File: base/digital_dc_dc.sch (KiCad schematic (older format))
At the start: 33 parts

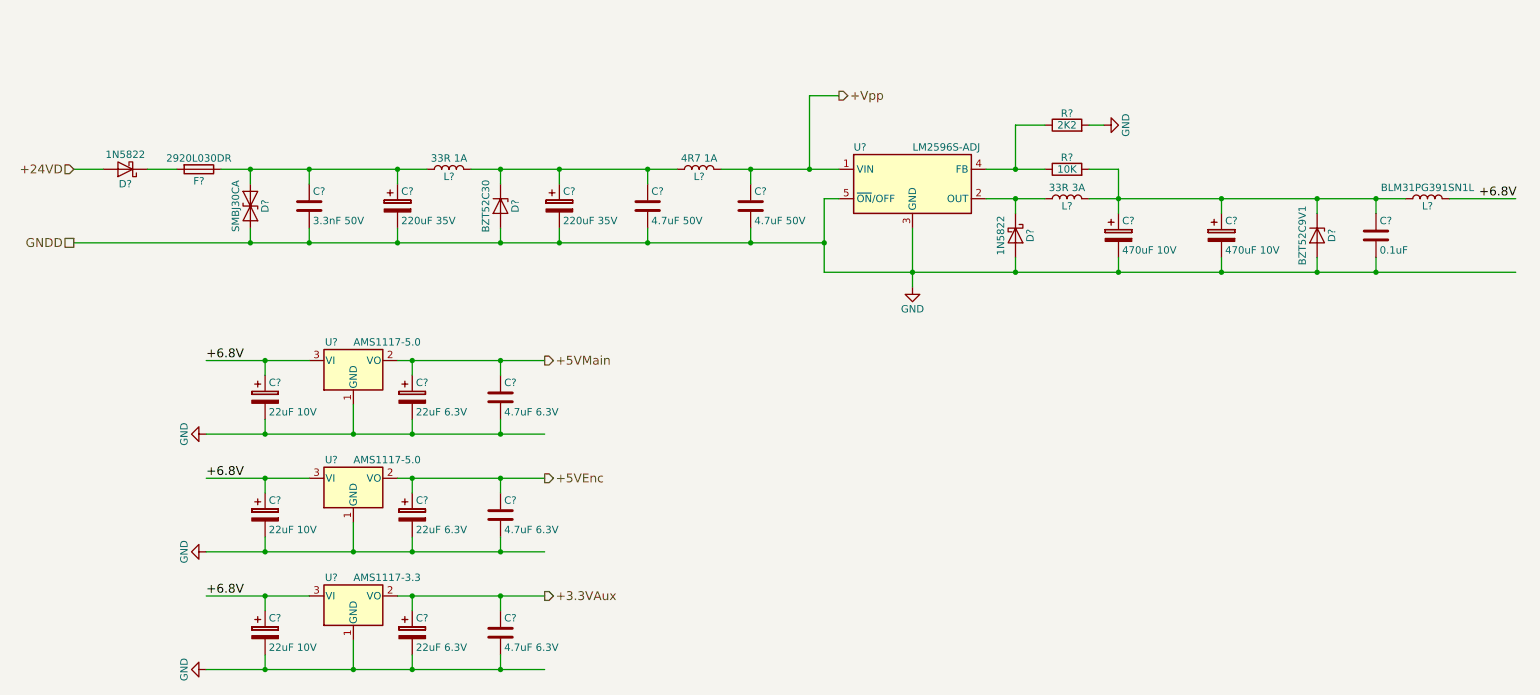
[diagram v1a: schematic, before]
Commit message: Update base board: 1. Add extra analog voltage input to core board.   -> update pinmux 2. Assign most footprints. 3. Generate netlist. 4. Add core_sf board. 5. Add kicad_symbols library submodule.
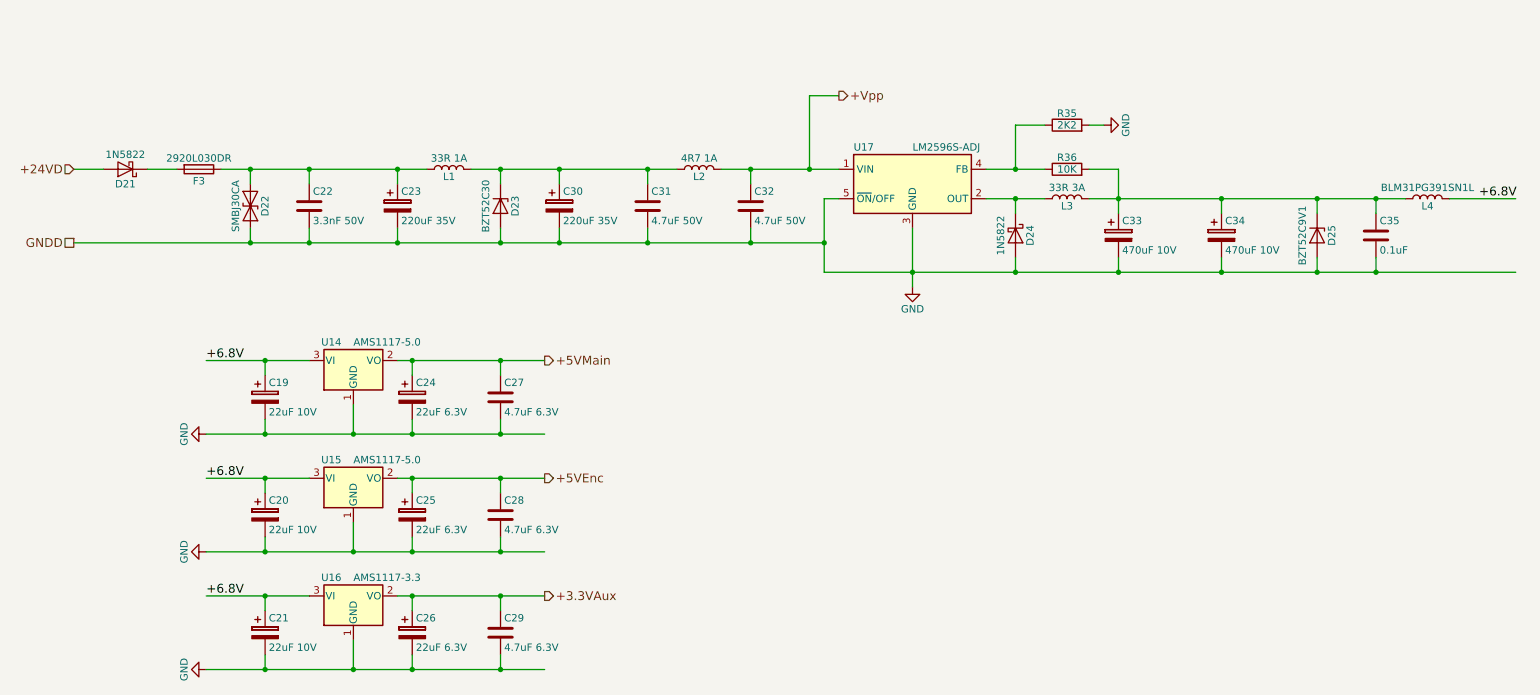
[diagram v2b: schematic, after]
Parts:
- gave numbers to parts that had none: 33
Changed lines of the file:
@@
 GNDD
 $Comp
-L 1N5822 D?
+L 1N5822 D21
 U 1 1 5A392E0A
 P 1550 3000
-F 0 "D?" H 1550 3100 50  0000 C CNN
+F 0 "D21" H 1550 3100 50  0000 C CNN
 F 1 "1N5822" H 1550 2900 50  0000 C CNN
 F 2 "Diode_SMD:D_SMA" H 1550 2825 50  0001 C CNN
@@
 $EndComp
 $Comp
-L Fuse F?
+L Fuse F3
 U 1 1 5A392F16
 P 2050 3000
-F 0 "F?" V 2130 3000 50  0000 C CNN
+F 0 "F3" V 2130 3000 50  0000 C CNN
 F 1 "2920L030DR" V 1975 3000 50  0000 C CNN
 F 2 "Fuse:Fuse_2920_7451Metric" V 1980 3000 50  0001 C CNN
@@
 $EndComp
 $Comp
-L D_TVS D?
+L D_TVS D22
 U 1 1 5A3934E7
 P 2400 3250
-F 0 "D?" H 2400 3350 50  0000 C CNN
+F 0 "D22" H 2400 3350 50  0000 C CNN
 F 1 "SMBJ30CA" H 2400 3150 50  0000 C CNN
 F 2 "Diode_SMD:D_SMB" H 2400 3250 50  0001 C CNN
@@
 $EndComp
 $Comp
-L C C?
+L C C22
 U 1 1 5A393804
 P 2800 3250
-F 0 "C?" H 2825 3350 50  0000 L CNN
+F 0 "C22" H 2825 3350 50  0000 L CNN
 F 1 "3.3nF 50V" H 2825 3150 50  0000 L CNN
 F 2 "Capacitor_SMD:C_0603_1608Metric" H 2838 3100 50  0001 C CNN
@@
 $EndComp
 $Comp
-L CP C?
+L CP C23
 U 1 1 5A393B3D
 P 3400 3250
-F 0 "C?" H 3425 3350 50  0000 L CNN
+F 0 "C23" H 3425 3350 50  0000 L CNN
 F 1 "220uF 35V" H 3425 3150 50  0000 L CNN
 F 2 "Capacitor_SMD:CP_Elec_8x10" H 3438 3100 50  0001 C CNN
@@
 $EndComp
 $Comp
-L L L?
+L L L1
 U 1 1 5A3940E0
 P 3750 3000
-F 0 "L?" V 3700 3000 50  0000 C CNN
+F 0 "L1" V 3700 3000 50  0000 C CNN
 F 1 "33R 1A" V 3825 3000 50  0000 C CNN
 F 2 "Inductor_SMD:L_7.3x7.3_H3.5" H 3750 3000 50  0001 C CNN
@@
 $EndComp
 $Comp
-L D_Zener D?
+L D_Zener D23
 U 1 1 5A394214
 P 4100 3250
-F 0 "D?" H 4100 3350 50  0000 C CNN
+F 0 "D23" H 4100 3350 50  0000 C CNN
 F 1 "BZT52C30" H 4100 3150 50  0000 C CNN
 F 2 "Diode_SMD:D_SOD-123" H 4100 3250 50  0001 C CNN
@@
 $EndComp
 $Comp
-L CP C?
+L CP C30
 U 1 1 5A394320
 P 4500 3250
-F 0 "C?" H 4525 3350 50  0000 L CNN
+F 0 "C30" H 4525 3350 50  0000 L CNN
 F 1 "220uF 35V" H 4525 3150 50  0000 L CNN
 F 2 "Capacitor_SMD:CP_Elec_8x10" H 4538 3100 50  0001 C CNN
@@
 $EndComp
 $Comp
-L C C?
+L C C31
 U 1 1 5A394607
 P 5100 3250
-F 0 "C?" H 5125 3350 50  0000 L CNN
+F 0 "C31" H 5125 3350 50  0000 L CNN
 F 1 "4.7uF 50V" H 5125 3150 50  0000 L CNN
 F 2 "Capacitor_SMD:C_1210_3225Metric" H 5138 3100 50  0001 C CNN
@@
 $EndComp
 $Comp
-L L L?
+L L L2
 U 1 1 5A394796
 P 5450 3000
-F 0 "L?" V 5400 3000 50  0000 C CNN
+F 0 "L2" V 5400 3000 50  0000 C CNN
 F 1 "4R7 1A" V 5525 3000 50  0000 C CNN
 F 2 "Inductor_SMD:L_Taiyo-Yuden_MD-3030" H 5450 3000 50  0001 C CNN
@@
 $EndComp
 $Comp
-L C C?
+L C C32
 U 1 1 5A394844
 P 5800 3250
-F 0 "C?" H 5825 3350 50  0000 L CNN
+F 0 "C32" H 5825 3350 50  0000 L CNN
 F 1 "4.7uF 50V" H 5825 3150 50  0000 L CNN
 F 2 "Capacitor_SMD:C_1210_3225Metric" H 5838 3100 50  0001 C CNN
@@
 $EndComp
 $Comp
-L LM2596S-ADJ U?
+L LM2596S-ADJ U17
 U 1 1 5A395D36
 P 6900 3100
-F 0 "U?" H 6500 3350 50  0000 L CNN
+F 0 "U17" H 6500 3350 50  0000 L CNN
 F 1 "LM2596S-ADJ" H 6900 3350 50  0000 L CNN
 F 2 "Package_TO_SOT_SMD:TO-263-5_TabPin3" H 6950 2850 50  0001 L CIN
@@
 $EndComp
 $Comp
-L 1N5822 D?
+L 1N5822 D24
 U 1 1 5A395F02
 P 7600 3450
-F 0 "D?" H 7600 3550 50  0000 C CNN
+F 0 "D24" H 7600 3550 50  0000 C CNN
 F 1 "1N5822" H 7600 3350 50  0000 C CNN
 F 2 "Diode_SMD:D_SMA" H 7600 3275 50  0001 C CNN
@@
 $EndComp
 $Comp
-L L L?
+L L L3
 U 1 1 5A396123
 P 7950 3200
-F 0 "L?" V 7900 3200 50  0000 C CNN
+F 0 "L3" V 7900 3200 50  0000 C CNN
 F 1 "33R 3A" V 8025 3200 50  0000 C CNN
 F 2 "Inductor_SMD:L_12x12mm_h8mm" H 7950 3200 50  0001 C CNN
@@
 $EndComp
 $Comp
-L R R?
+L R R36
 U 1 1 5A396200
 P 7950 3000
-F 0 "R?" V 8030 3000 50  0000 C CNN
+F 0 "R36" V 8030 3000 50  0000 C CNN
 F 1 "10K" V 7950 3000 50  0000 C CNN
 F 2 "Resistor_SMD:R_0603_1608Metric" V 7880 3000 50  0001 C CNN
@@
 $EndComp
 $Comp
-L R R?
+L R R35
 U 1 1 5A396375
 P 7950 2700
-F 0 "R?" V 8030 2700 50  0000 C CNN
+F 0 "R35" V 8030 2700 50  0000 C CNN
 F 1 "2K2" V 7950 2700 50  0000 C CNN
 F 2 "Resistor_SMD:R_0603_1608Metric" V 7880 2700 50  0001 C CNN
@@
 $EndComp
 $Comp
-L GND #PWR?
+L GND #PWR020
 U 1 1 5A3963F4
 P 6900 3800
-F 0 "#PWR?" H 6900 3550 50  0001 C CNN
+F 0 "#PWR020" H 6900 3550 50  0001 C CNN
 F 1 "GND" H 6900 3650 50  0000 C CNN
 F 2 "" H 6900 3800 50  0001 C CNN
@@
 $EndComp
 $Comp
-L GND #PWR?
+L GND #PWR021
 U 1 1 5A3964B9
 P 8200 2700
-F 0 "#PWR?" H 8200 2450 50  0001 C CNN
+F 0 "#PWR021" H 8200 2450 50  0001 C CNN
 F 1 "GND" H 8200 2550 50  0000 C CNN
 F 2 "" H 8200 2700 50  0001 C CNN
@@
 $EndComp
 $Comp
-L CP C?
+L CP C33
 U 1 1 5A3964F4
 P 8300 3450
-F 0 "C?" H 8325 3550 50  0000 L CNN
+F 0 "C33" H 8325 3550 50  0000 L CNN
 F 1 "470uF 10V" H 8325 3350 50  0000 L CNN
 F 2 "Capacitor_SMD:CP_Elec_8x10" H 8338 3300 50  0001 C CNN
@@
 $EndComp
 $Comp
-L D_Zener D?
+L D_Zener D25
 U 1 1 5A396751
 P 9650 3450
-F 0 "D?" H 9650 3550 50  0000 C CNN
+F 0 "D25" H 9650 3550 50  0000 C CNN
 F 1 "BZT52C9V1" H 9650 3350 50  0000 C CNN
 F 2 "Diode_SMD:D_SOD-123" H 9650 3450 50  0001 C CNN
@@
 $EndComp
 $Comp
-L C C?
+L C C35
 U 1 1 5A396963
 P 10050 3450
-F 0 "C?" H 10075 3550 50  0000 L CNN
+F 0 "C35" H 10075 3550 50  0000 L CNN
 F 1 "0.1uF" H 10075 3350 50  0000 L CNN
 F 2 "Capacitor_SMD:C_0603_1608Metric" H 10088 3300 50  0001 C CNN
@@
 $EndComp
 $Comp
-L L L?
+L L L4
 U 1 1 5A396C17
 P 10400 3200
-F 0 "L?" V 10350 3200 50  0000 C CNN
+F 0 "L4" V 10350 3200 50  0000 C CNN
 F 1 "BLM31PG391SN1L" V 10475 3200 50  0000 C CNN
 F 2 "Inductor_SMD:L_1206_3216Metric" H 10400 3200 50  0001 C CNN
@@
 +6.8V
 $Comp
-L CP C?
+L CP C19
 U 1 1 5A3971EB
 P 2500 4550
-F 0 "C?" H 2525 4650 50  0000 L CNN
+F 0 "C19" H 2525 4650 50  0000 L CNN
 F 1 "22uF 10V" H 2525 4450 50  0000 L CNN
 F 2 "Capacitor_Tantalum_SMD:CP_EIA-3216-18_Kemet-A" H 2538 4400 50  0001 C CNN
@@
 $EndComp
 $Comp
-L AP1117-15 U?
+L AP1117-15 U14
 U 1 1 5A398264
 P 3100 4300
-F 0 "U?" H 2950 4425 50  0000 C CNN
+F 0 "U14" H 2950 4425 50  0000 C CNN
 F 1 "AMS1117-5.0" H 3100 4425 50  0000 L CNN
 F 2 "Package_TO_SOT_SMD:SOT-223" H 3100 4500 50  0001 C CNN
@@
 +6.8V
 $Comp
-L GND #PWR?
+L GND #PWR022
 U 1 1 5A3987CE
 P 2100 4800
-F 0 "#PWR?" H 2100 4550 50  0001 C CNN
+F 0 "#PWR022" H 2100 4550 50  0001 C CNN
 F 1 "GND" H 2100 4650 50  0000 C CNN
 F 2 "" H 2100 4800 50  0001 C CNN
@@
 $EndComp
 $Comp
-L CP C?
+L CP C24
 U 1 1 5A3988D5
 P 3500 4550
-F 0 "C?" H 3525 4650 50  0000 L CNN
+F 0 "C24" H 3525 4650 50  0000 L CNN
 F 1 "22uF 6.3V" H 3525 4450 50  0000 L CNN
 F 2 "Capacitor_Tantalum_SMD:CP_EIA-3216-18_Kemet-A" H 3538 4400 50  0001 C CNN
@@
 $EndComp
 $Comp
-L C C?
+L C C27
 U 1 1 5A398AEE
 P 4100 4550
-F 0 "C?" H 4125 4650 50  0000 L CNN
+F 0 "C27" H 4125 4650 50  0000 L CNN
 F 1 "4.7uF 6.3V" H 4125 4450 50  0000 L CNN
 F 2 "Capacitor_SMD:C_0603_1608Metric" H 4138 4400 50  0001 C CNN
@@
 $EndComp
 $Comp
-L CP C?
+L CP C20
 U 1 1 5A398DF8
 P 2500 5350
-F 0 "C?" H 2525 5450 50  0000 L CNN
+F 0 "C20" H 2525 5450 50  0000 L CNN
 F 1 "22uF 10V" H 2525 5250 50  0000 L CNN
 F 2 "Capacitor_Tantalum_SMD:CP_EIA-3216-18_Kemet-A" H 2538 5200 50  0001 C CNN
@@
 $EndComp
 $Comp
-L AP1117-15 U?
+L AP1117-15 U15
 U 1 1 5A398DFE
 P 3100 5100
-F 0 "U?" H 2950 5225 50  0000 C CNN
+F 0 "U15" H 2950 5225 50  0000 C CNN
 F 1 "AMS1117-5.0" H 3100 5225 50  0000 L CNN
 F 2 "Package_TO_SOT_SMD:SOT-223" H 3100 5300 50  0001 C CNN
@@
 +6.8V
 $Comp
-L GND #PWR?
+L GND #PWR023
 U 1 1 5A398E0C
 P 2100 5600
-F 0 "#PWR?" H 2100 5350 50  0001 C CNN
+F 0 "#PWR023" H 2100 5350 50  0001 C CNN
 F 1 "GND" H 2100 5450 50  0000 C CNN
 F 2 "" H 2100 5600 50  0001 C CNN
@@
 $EndComp
 $Comp
-L CP C?
+L CP C25
 U 1 1 5A398E13
 P 3500 5350
-F 0 "C?" H 3525 5450 50  0000 L CNN
+F 0 "C25" H 3525 5450 50  0000 L CNN
 F 1 "22uF 6.3V" H 3525 5250 50  0000 L CNN
 F 2 "Capacitor_Tantalum_SMD:CP_EIA-3216-18_Kemet-A" H 3538 5200 50  0001 C CNN
@@
 $EndComp
 $Comp
-L C C?
+L C C28
 U 1 1 5A398E1E
 P 4100 5350
-F 0 "C?" H 4125 5450 50  0000 L CNN
+F 0 "C28" H 4125 5450 50  0000 L CNN
 F 1 "4.7uF 6.3V" H 4125 5250 50  0000 L CNN
 F 2 "Capacitor_SMD:C_0603_1608Metric" H 4138 5200 50  0001 C CNN
@@
 $EndComp
 $Comp
-L CP C?
+L CP C21
 U 1 1 5A398F3C
 P 2500 6150
-F 0 "C?" H 2525 6250 50  0000 L CNN
+F 0 "C21" H 2525 6250 50  0000 L CNN
 F 1 "22uF 10V" H 2525 6050 50  0000 L CNN
 F 2 "Capacitor_Tantalum_SMD:CP_EIA-3216-18_Kemet-A" H 2538 6000 50  0001 C CNN
@@
 $EndComp
 $Comp
-L AP1117-15 U?
+L AP1117-15 U16
 U 1 1 5A398F42
 P 3100 5900
-F 0 "U?" H 2950 6025 50  0000 C CNN
+F 0 "U16" H 2950 6025 50  0000 C CNN
 F 1 "AMS1117-3.3" H 3100 6025 50  0000 L CNN
 F 2 "Package_TO_SOT_SMD:SOT-223" H 3100 6100 50  0001 C CNN
@@
 +6.8V
 $Comp
-L GND #PWR?
+L GND #PWR024
 U 1 1 5A398F50
 P 2100 6400
-F 0 "#PWR?" H 2100 6150 50  0001 C CNN
+F 0 "#PWR024" H 2100 6150 50  0001 C CNN
 F 1 "GND" H 2100 6250 50  0000 C CNN
 F 2 "" H 2100 6400 50  0001 C CNN
@@
 $EndComp
 $Comp
-L CP C?
+L CP C26
 U 1 1 5A398F57
 P 3500 6150
-F 0 "C?" H 3525 6250 50  0000 L CNN
+F 0 "C26" H 3525 6250 50  0000 L CNN
 F 1 "22uF 6.3V" H 3525 6050 50  0000 L CNN
 F 2 "Capacitor_Tantalum_SMD:CP_EIA-3216-18_Kemet-A" H 3538 6000 50  0001 C CNN
@@
 $EndComp
 $Comp
-L C C?
+L C C29
 U 1 1 5A398F62
 P 4100 6150
-F 0 "C?" H 4125 6250 50  0000 L CNN
+F 0 "C29" H 4125 6250 50  0000 L CNN
 F 1 "4.7uF 6.3V" H 4125 6050 50  0000 L CNN
 F 2 "Capacitor_SMD:C_0603_1608Metric" H 4138 6000 50  0001 C CNN
@@
 $EndComp
 $Comp
-L CP C?
+L CP C34
 U 1 1 5A3A1070
 P 9000 3450
-F 0 "C?" H 9025 3550 50  0000 L CNN
+F 0 "C34" H 9025 3550 50  0000 L CNN
 F 1 "470uF 10V" H 9025 3350 50  0000 L CNN
 F 2 "Capacitor_SMD:CP_Elec_8x10" H 9038 3300 50  0001 C CNN

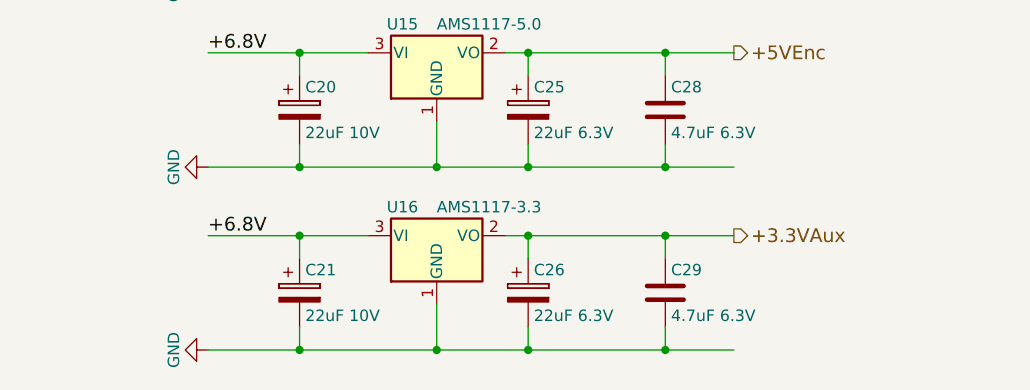
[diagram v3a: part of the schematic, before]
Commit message: Update footprints.
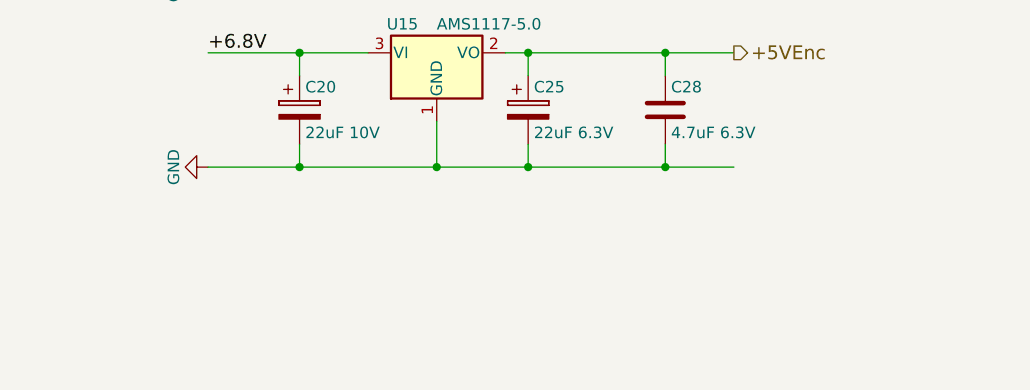
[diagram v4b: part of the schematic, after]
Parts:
- removed C21: 22uF 10V, Capacitor_Tantalum_SMD:CP_EIA-3216-18_Kemet-A, symbol CP
- removed C26: 22uF 6.3V, Capacitor_Tantalum_SMD:CP_EIA-3216-18_Kemet-A, symbol CP
- removed C29: 4.7uF 6.3V, Capacitor_SMD:C_0603_1608Metric, symbol C
- removed U16: AMS1117-3.3, Package_TO_SOT_SMD:SOT-223, symbol AP1117-15
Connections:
- net labels removed: +3.3VAux
- wire segments 74 -> 64
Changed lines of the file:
@@
 Text HLabel 4400 4300 2    60   Output ~ 0
 +5VMain
-Text HLabel 4400 5900 2    60   Output ~ 0
-+3.3VAux
 Text HLabel 1200 3500 0    60   UnSpc ~ 0
 GNDD
@@
 $EndComp
 $Comp
-L CP C21
-U 1 1 5A398F3C
-P 2500 6150
-F 0 "C21" H 2525 6250 50  0000 L CNN
-F 1 "22uF 10V" H 2525 6050 50  0000 L CNN
-F 2 "Capacitor_Tantalum_SMD:CP_EIA-3216-18_Kemet-A" H 2538 6000 50  0001 C CNN
-F 3 "" H 2500 6150 50  0001 C CNN
-	1    2500 6150
-	1    0    0    -1
-$EndComp
-$Comp
-L AP1117-15 U16
-U 1 1 5A398F42
-P 3100 5900
-F 0 "U16" H 2950 6025 50  0000 C CNN
-F 1 "AMS1117-3.3" H 3100 6025 50  0000 L CNN
-F 2 "Package_TO_SOT_SMD:SOT-223" H 3100 6100 50  0001 C CNN
-F 3 "" H 3200 5650 50  0001 C CNN
-	1    3100 5900
-	1    0    0    -1
-$EndComp
-Text Label 2100 5900 0    60   ~ 0
-+6.8V
-$Comp
-L GND #PWR024
-U 1 1 5A398F50
-P 2100 6400
-F 0 "#PWR024" H 2100 6150 50  0001 C CNN
-F 1 "GND" H 2100 6250 50  0000 C CNN
-F 2 "" H 2100 6400 50  0001 C CNN
-F 3 "" H 2100 6400 50  0001 C CNN
-	1    2100 6400
-	0    1    1    0
-$EndComp
-$Comp
-L CP C26
-U 1 1 5A398F57
-P 3500 6150
-F 0 "C26" H 3525 6250 50  0000 L CNN
-F 1 "22uF 6.3V" H 3525 6050 50  0000 L CNN
-F 2 "Capacitor_Tantalum_SMD:CP_EIA-3216-18_Kemet-A" H 3538 6000 50  0001 C CNN
-F 3 "" H 3500 6150 50  0001 C CNN
-	1    3500 6150
-	1    0    0    -1
-$EndComp
-$Comp
-L C C29
-U 1 1 5A398F62
-P 4100 6150
-F 0 "C29" H 4125 6250 50  0000 L CNN
-F 1 "4.7uF 6.3V" H 4125 6050 50  0000 L CNN
-F 2 "Capacitor_SMD:C_0603_1608Metric" H 4138 6000 50  0001 C CNN
-F 3 "" H 4100 6150 50  0001 C CNN
-	1    4100 6150
-	1    0    0    -1
-$EndComp
-$Comp
 L CP C34
 U 1 1 5A3A1070
@@
 Connection ~ 4100 5600
 Wire Wire Line
-	2500 6300 2500 6400
-Wire Wire Line
-	2100 6400 4400 6400
-Wire Wire Line
-	3100 6400 3100 6200
-Connection ~ 2500 6400
-Wire Wire Line
-	2100 5900 2800 5900
-Wire Wire Line
-	2500 5900 2500 6000
-Connection ~ 2500 5900
-Connection ~ 3100 6400
-Wire Wire Line
-	3400 5900 4400 5900
-Wire Wire Line
-	3500 5900 3500 6000
-Wire Wire Line
-	3500 6300 3500 6400
-Connection ~ 3500 6400
-Connection ~ 3500 5900
-Wire Wire Line
-	4100 6000 4100 5900
-Connection ~ 4100 5900
-Wire Wire Line
-	4100 6300 4100 6400
-Connection ~ 4100 6400
-Wire Wire Line
 	9000 3700 9000 3600
